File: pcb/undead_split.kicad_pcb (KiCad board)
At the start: 2 copper layers, 356.8 x 105 mm, 181 parts, among them J1 USB_C_Receptacle_USB2.0, J2 USB_C_Receptacle_USB2.0, J3 USB_C_Receptacle_USB2.0, J4 USB_C_Receptacle_USB2.0, SW1 SW_Push, SW10 SW_Push, SW11 SW_Push, SW12 SW_Push, SW13 SW_Push, SW14 SW_Push, SW15 SW_Push, SW16 SW_Push, SW17 SW_Push, SW18 SW_Push, SW19 SW_Push, SW2 SW_Push, SW20 SW_Push, SW21 SW_Push, SW22 SW_Push, SW23 SW_Push, SW24 SW_Push, SW25 SW_Push, SW26 SW_Push, SW27 SW_Push, SW28 SW_Push, SW29 SW_Push, SW3 SW_Push, SW30 SW_Push, SW31 SW_Push, SW32 SW_Push, SW33 SW_Push, SW34 SW_Push, SW35 SW_Push, SW36 SW_Push, SW37 SW_Push, SW38 SW_Push, SW39 SW_Push, SW4 SW_Push, SW40 SW_Push, SW41 SW_Push, SW42 SW_Push, SW43 SW_Push, SW44 SW_Push, SW45 SW_Push, SW46 SW_Push, SW47 SW_Push, SW48 SW_Push, SW49 SW_Push, SW5 SW_Push, SW50 SW_Push, SW51 SW_Push, SW52 SW_Push, SW53 SW_Push, SW54 SW_Push, SW55 SW_Push, SW56 SW_Push, SW57 SW_Push, SW58 SW_Push, SW59 SW_Push, SW6 SW_Push, SW60 SW_Push, SW7 SW_Push, SW8 SW_Push, SW9 SW_Push, U1 ATmega32U4-A, U2 ATmega32U4-A

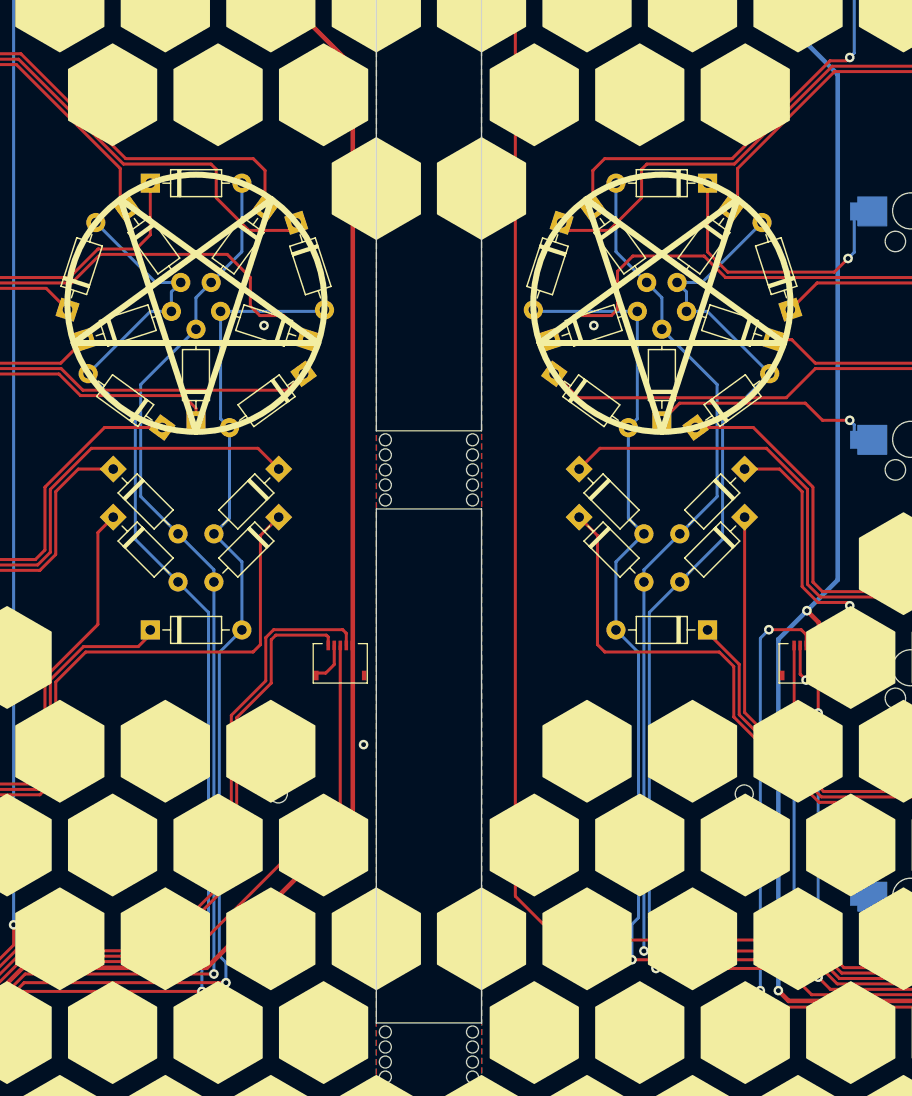
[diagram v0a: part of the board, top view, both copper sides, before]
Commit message: Fix vertical joycon alignment
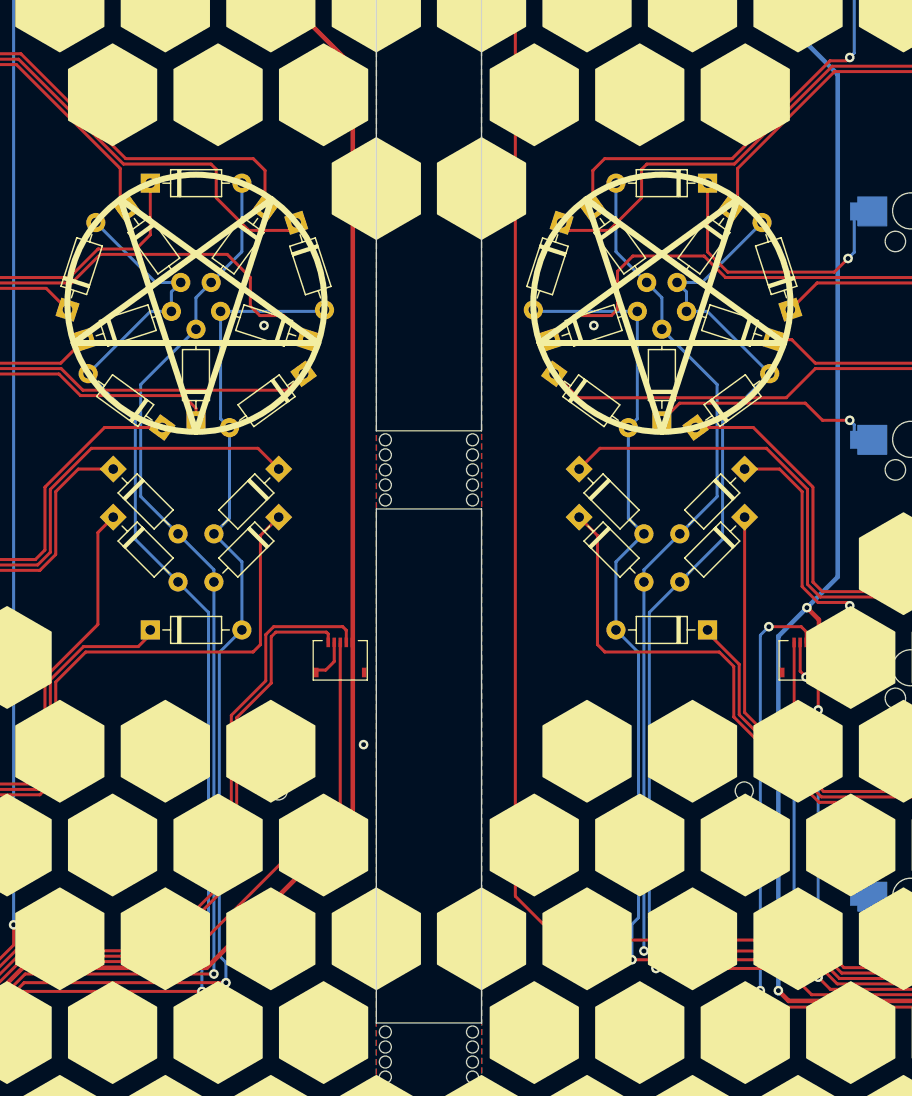
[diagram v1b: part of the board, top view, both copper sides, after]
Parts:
- moved JOY1 0.25 mm to (205.8, 162.5)
- moved JOY2 0.25 mm to (244.6, 162.5)
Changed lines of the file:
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@@
 	(footprint "footprints:joycon_joystick"
 		(layer "F.Cu")
-		(at 205.833462 162.788198)
+		(at 205.833462 162.538198)
 		(descr "Molex FFC & FPC connector, 05 top-side contacts, 0.5mm pitch, SMT, https://wmsc.lcsc.com/wmsc/upload/file/pdf/v2/lcsc/2210261730_HCTL-HC-FPC-05-09-5RLTAG_C5213747.pdf")
 		(tags "molex ffc fpc 51281-0598")
@@
 	(footprint "footprints:joycon_joystick"
 		(layer "F.Cu")
-		(at 244.583462 162.788198)
+		(at 244.583462 162.538198)
 		(descr "Molex FFC & FPC connector, 05 top-side contacts, 0.5mm pitch, SMT, https://wmsc.lcsc.com/wmsc/upload/file/pdf/v2/lcsc/2210261730_HCTL-HC-FPC-05-09-5RLTAG_C5213747.pdf")
 		(tags "molex ffc fpc 51281-0598")
@@
 	)
 	(segment
-		(start 205.333462 163.128198)
-		(end 204.623462 163.838198)
+		(start 205.333462 162.878198)
+		(end 204.623462 163.588198)
 		(width 0.25)
 		(layer "F.Cu")
@@
 	)
 	(segment
-		(start 204.623462 163.838198)
-		(end 203.933462 163.838198)
+		(start 204.623462 163.588198)
+		(end 203.933462 163.588198)
 		(width 0.25)
 		(layer "F.Cu")
@@
 	)
 	(segment
-		(start 205.333462 163.128198)
-		(end 205.333462 161.538198)
+		(start 205.333462 162.878198)
+		(end 205.333462 161.288198)
 		(width 0.25)
 		(layer "F.Cu")
@@
 	)
 	(segment
-		(start 200.480462 160.679198)
-		(end 200.090991 161.068669)
+		(start 200.480462 160.429198)
+		(end 200.090991 160.818669)
 		(width 0.25)
 		(layer "F.Cu")
@@
 	)
 	(segment
-		(start 204.833462 160.833462)
-		(end 204.679198 160.679198)
+		(start 204.833462 160.583462)
+		(end 204.679198 160.429198)
 		(width 0.25)
 		(layer "F.Cu")
@@
 	)
 	(segment
-		(start 204.679198 160.679198)
-		(end 200.480462 160.679198)
+		(start 204.679198 160.429198)
+		(end 200.480462 160.429198)
 		(width 0.25)
 		(layer "F.Cu")
@@
 	)
 	(segment
-		(start 204.833462 161.538198)
-		(end 204.833462 160.833462)
+		(start 204.833462 161.288198)
+		(end 204.833462 160.583462)
 		(width 0.25)
 		(layer "F.Cu")
@@
 	)
 	(segment
-		(start 200.090991 161.068669)
+		(start 200.090991 160.818669)
 		(end 200.090991 164.670503)
 		(width 0.25)
@@
 	(segment
 		(start 205.833462 174.734753)
-		(end 205.833462 161.538198)
+		(end 205.833462 161.288198)
 		(width 0.25)
 		(layer "F.Cu")
@@
 	)
 	(segment
-		(start 199.640991 160.882273)
-		(end 200.294066 160.229198)
+		(start 199.640991 160.632273)
+		(end 200.294066 159.979198)
 		(width 0.25)
 		(layer "F.Cu")
@@
 	)
 	(segment
-		(start 206.03766 160.229198)
-		(end 206.333462 160.525)
+		(start 206.03766 159.979198)
+		(end 206.333462 160.275)
 		(width 0.25)
 		(layer "F.Cu")
@@
 	(segment
 		(start 199.640991 164.484107)
-		(end 199.640991 160.882273)
+		(end 199.640991 160.632273)
 		(width 0.25)
 		(layer "F.Cu")
@@
 	)
 	(segment
-		(start 206.333462 160.525)
-		(end 206.333462 161.538198)
+		(start 206.333462 160.275)
+		(end 206.333462 161.288198)
 		(width 0.25)
 		(layer "F.Cu")
@@
 	)
 	(segment
-		(start 200.294066 160.229198)
-		(end 206.03766 160.229198)
+		(start 200.294066 159.979198)
+		(end 206.03766 159.979198)
 		(width 0.25)
 		(layer "F.Cu")
@@
 	)
 	(segment
-		(start 243.583462 161.538198)
-		(end 243.583462 167.163198)
+		(start 243.583462 161.288198)
+		(end 243.583462 166.913198)
 		(width 0.25)
 		(layer "F.Cu")
@@
 	)
 	(via
-		(at 243.583462 167.163198)
+		(at 243.583462 166.913198)
 		(size 0.8)
 		(drill 0.4)
@@
 	)
 	(segment
-		(start 243.583462 167.163198)
+		(start 243.583462 166.913198)
 		(end 243.583462 189.131056)
 		(width 0.25)
@@
 	)
 	(segment
-		(start 241.480306 160.229901)
-		(end 244.175165 160.229901)
+		(start 241.480306 159.979901)
+		(end 244.175165 159.979901)
 		(width 0.25)
 		(layer "F.Cu")
@@
 	)
 	(segment
-		(start 244.175165 160.229901)
-		(end 244.583462 160.638198)
+		(start 244.175165 159.979901)
+		(end 244.583462 160.388198)
 		(width 0.25)
 		(layer "F.Cu")
@@
 	)
 	(segment
-		(start 244.583462 160.638198)
-		(end 244.583462 161.538198)
+		(start 244.583462 160.388198)
+		(end 244.583462 161.288198)
 		(width 0.25)
 		(layer "F.Cu")
@@
 	)
 	(via
-		(at 241.480306 160.229901)
+		(at 241.480306 159.979901)
 		(size 0.8)
 		(drill 0.4)
@@
 	(segment
 		(start 240.771973 190.24658)
-		(end 240.771973 160.938234)
+		(end 240.771973 160.688234)
 		(width 0.25)
 		(layer "B.Cu")
@@
 	)
 	(segment
-		(start 240.771973 160.938234)
-		(end 241.480306 160.229901)
+		(start 240.771973 160.688234)
+		(end 241.480306 159.979901)
 		(width 0.25)
 		(layer "B.Cu")
@@
 	)
 	(segment
-		(start 245.083462 162.896569)
-		(end 245.083462 161.538198)
+		(start 245.083462 162.646569)
+		(end 245.083462 161.288198)
 		(width 0.25)
 		(layer "F.Cu")
@@
 	)
 	(segment
-		(start 245.583462 163.396569)
-		(end 245.583462 167.163198)
+		(start 245.583462 163.146569)
+		(end 245.583462 166.913198)
 		(width 0.25)
 		(layer "F.Cu")
@@
 	)
 	(segment
-		(start 245.083462 162.896569)
-		(end 245.583462 163.396569)
+		(start 245.083462 162.646569)
+		(end 245.583462 163.146569)
 		(width 0.25)
 		(layer "F.Cu")
@@
 	)
 	(via
-		(at 245.583462 167.163198)
+		(at 245.583462 166.913198)
 		(size 0.8)
 		(drill 0.4)
@@
 	)
 	(segment
-		(start 245.583462 167.163198)
+		(start 245.583462 166.913198)
 		(end 245.583462 189.131056)
 		(width 0.25)
@@
 	)
 	(segment
-		(start 244.083462 161.538198)
-		(end 244.083462 163.927843)
+		(start 244.083462 161.288198)
+		(end 244.083462 163.677843)
 		(width 0.25)
 		(layer "F.Cu")
@@
 	)
 	(segment
-		(start 244.083462 163.927843)
-		(end 244.574843 164.419224)
+		(start 244.083462 163.677843)
+		(end 244.574843 164.169224)
 		(width 0.25)
 		(layer "F.Cu")
@@
 	)
 	(via
-		(at 244.574843 164.419224)
+		(at 244.574843 164.169224)
 		(size 0.8)
 		(drill 0.4)
@@
 	)
 	(segment
-		(start 245.648962 159.648555)
-		(end 245.648962 161.538198)
+		(start 245.648962 159.398555)
+		(end 245.648962 161.288198)
 		(width 0.381)
 		(layer "F.Cu")
@@
 	)
 	(segment
-		(start 244.646974 158.646567)
-		(end 245.648962 159.648555)
+		(start 244.646974 158.396567)
+		(end 245.648962 159.398555)
 		(width 0.381)
 		(layer "F.Cu")
@@
 	)
 	(via
-		(at 244.646974 158.646567)
+		(at 244.646974 158.396567)
 		(size 0.8)
 		(drill 0.4)
@@
 	(segment
 		(start 247.208641 114.046931)
-		(end 247.208641 156.0849)
+		(end 247.208641 155.8349)
 		(width 0.381)
 		(layer "B.Cu")
@@
 	)
 	(segment
-		(start 242.271973 161.021568)
-		(end 244.646974 158.646567)
+		(start 242.271973 160.771568)
+		(end 244.646974 158.396567)
 		(width 0.381)
 		(layer "B.Cu")
@@
 	)
 	(segment
-		(start 242.271973 190.24658)
-		(end 242.271973 161.021568)
+		(start 242.271973 190.49658)
+		(end 242.271973 160.771568)
 		(width 0.381)
 		(layer "B.Cu")
@@
 	)
 	(segment
-		(start 247.208641 156.0849)
-		(end 244.646974 158.646567)
+		(start 247.208641 155.8349)
+		(end 244.646974 158.396567)
 		(width 0.381)
 		(layer "B.Cu")
